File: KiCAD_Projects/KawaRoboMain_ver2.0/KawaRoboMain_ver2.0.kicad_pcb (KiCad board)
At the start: 2 copper layers, 65 x 75 mm, 128 parts, among them IC1 ATMEGA328P-A, P1 CONN_01X06, P10 CONN_01X02, P17 CONN_01X04, P19 CONN_01X01, P2 CONN_02X03, P21 CONN_01X01, P22 CONN_01X01, P3 CONN_01X06, P4 CONN_01X08, P5 CONN_01X06, P6 CONN_01X04, P7 CONN_01X01, P8 CONN_01X04, P9 CONN_01X03, Q1 MOSFET_N, Q10 MOSFET_N, Q11 MOSFET_N, Q12 MOSFET_N, Q13 MOSFET_N, Q14 MOSFET_N, Q17 MOSFET_N, Q2 MOSFET_N, Q3 MOSFET_N, Q4 MOSFET_N, Q5 MOSFET_N, Q6 MOSFET_N, Q7 MOSFET_N, Q8 MOSFET_N, Q9 MOSFET_N, SW1 SW_PUSH, SW2 SW_PUSH, SW3 SW_PUSH, SW6 SW_PUSH, SW7 SW_PUSH, U1 STM32F103_48, U10 NCP5359, U11 NCP5359, U15 NCP1117ST12T3G, U2 NCP1117ST33T3G, U3 NCP5359, U5 NCP5359, U8 NCP5359, U9 NCP5359, X1 CRYSTAL, X2 CRYSTAL

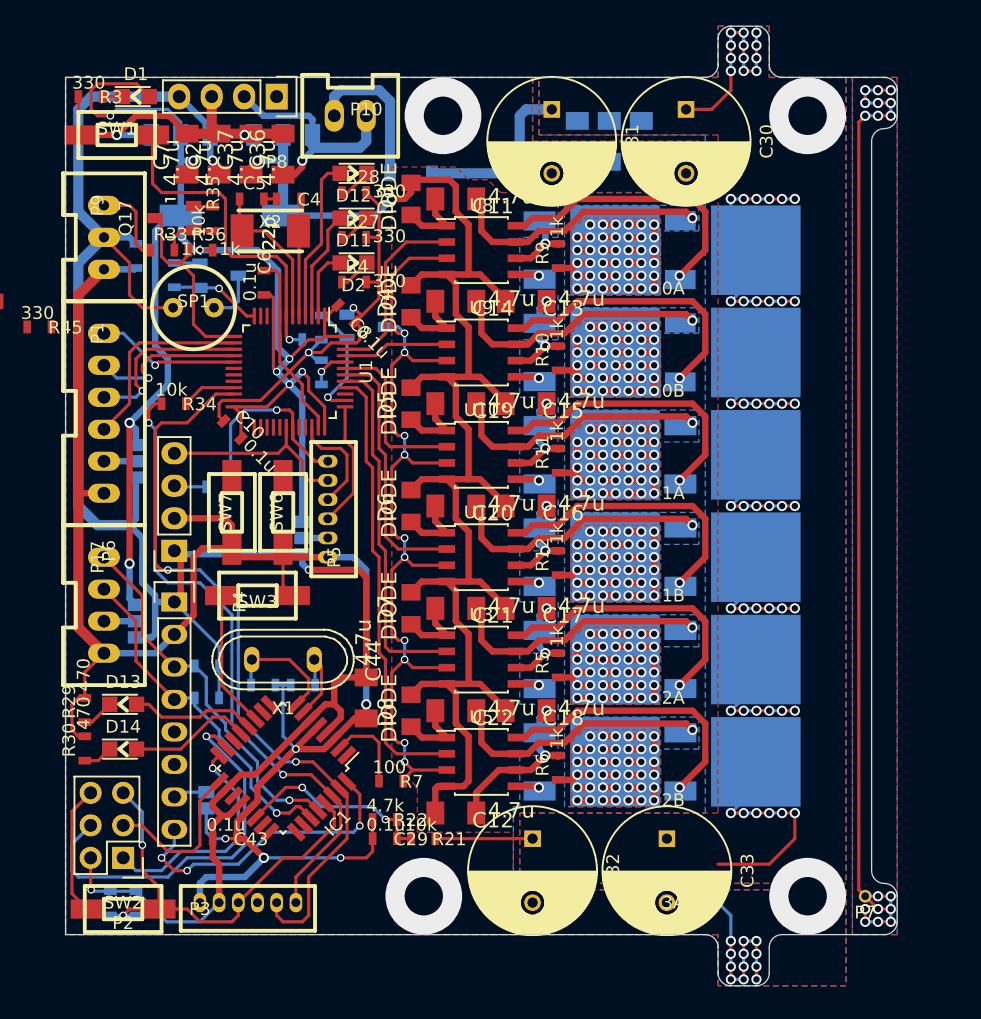
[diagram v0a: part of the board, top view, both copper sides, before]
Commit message: かわロボver2.0､中間電圧追加
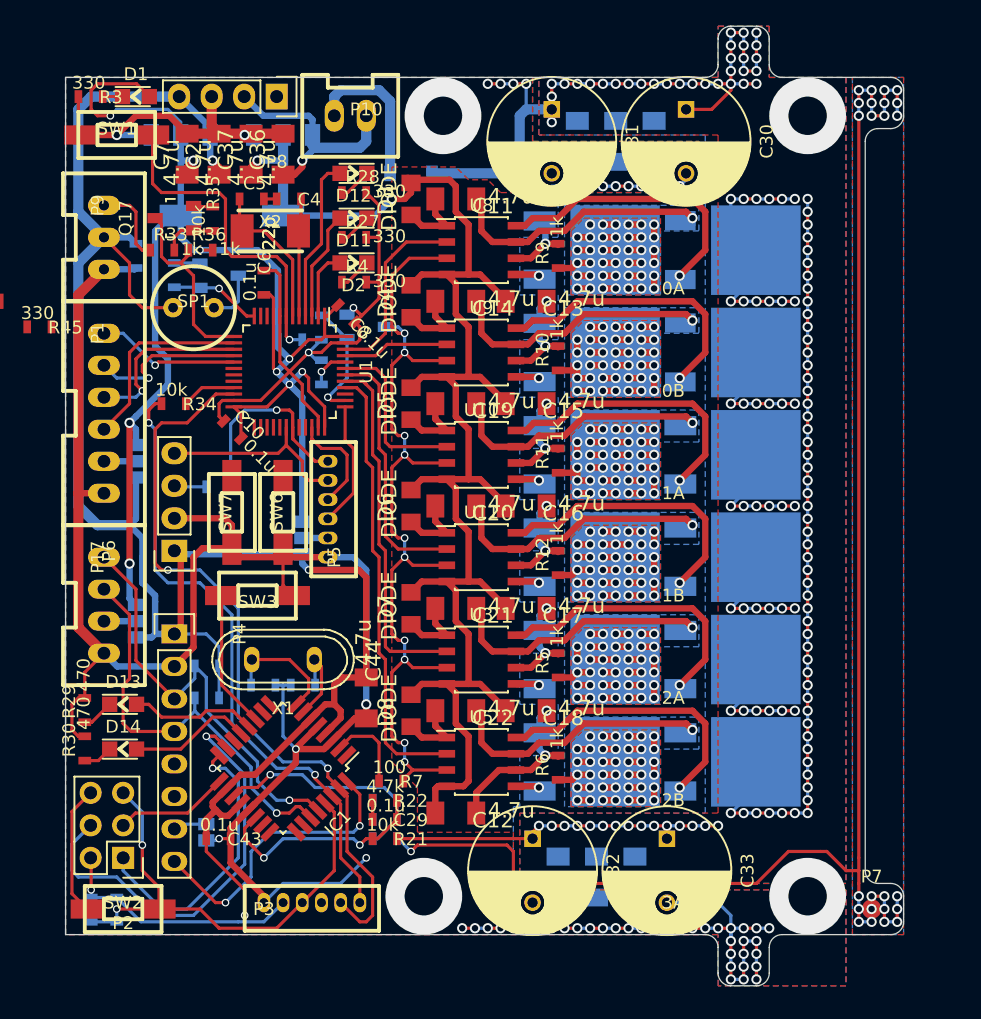
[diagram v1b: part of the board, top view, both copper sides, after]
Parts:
- added C1: 4.7u, RP_KiCAD_Libs:C3216_S, B.Cu at (60.5, 69.0)
- added C23: 0.1u, RP_KiCAD_Libs:C1608_WP_S, B.Cu at (41.0, 63.0)
- added C3: 4.7u, RP_KiCAD_Libs:C3216_S, B.Cu at (57.5, 69.0)
- added C9: 4.7u, RP_KiCAD_Libs:C3216_S, B.Cu at (54.5, 69.0)
- added R14: 4.7k, RP_KiCAD_Libs:C1608_WP_S, B.Cu at (41.0, 66.0)
- added R15: 4.7k, RP_KiCAD_Libs:C1608_WP_S, B.Cu at (41.0, 64.5)
- P7: footprint RP_KiCAD_Libs:testPin -> Measurement_Points:Measurement_Point_Round-SMD-Pad_Small
- moved P3 5.00 mm to (31.5, 71.0)
- moved R21 3.00 mm to (41.0, 66.0)
- moved JP1 2.50 mm to (27.0, 65.5)
- moved P4 2.50 mm to (24.5, 50.0)
- moved R19 1.58 mm to (18.0, 71.5)
- moved R32 1.58 mm to (20.0, 71.5)
- moved C29 1.50 mm to (41.0, 64.5)
- moved R22 1.50 mm to (41.0, 63.0)
- moved P7 1.12 mm to (79.0, 71.5)
- moved C40 1.00 mm to (62.0, 11.5)
- moved C43 0.50 mm to (28.0, 66.0)
- moved C45 0.50 mm to (59.0, 11.5)
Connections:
- IC1 pad 19: (no net) -> /cell_voltage
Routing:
- net +BATT: track 114.9 -> 197.3 mm, vias 54 -> 141
- net /BATT-SP: track 78.8 -> 123.8 mm, vias 18 -> 25
- net GND: track 305.4 -> 339.4 mm, vias 32 -> 66
- net /cell_voltage: track 0.00 -> 18.3 mm, vias 0 -> 1
- net +5V: track 166.4 -> 177.0 mm, vias 3 -> 4
- net /I2C_SDA: track 27.6 -> 32.9 mm
- net /SPI_MISO: track 18.7 -> 23.3 mm
- net /I2C_SCL: track 29.3 -> 33.6 mm
- net /SPI_SCK: track 12.7 -> 8.94 mm
- net /SPI_MOSI: track 31.3 -> 34.6 mm
- net /AT_RST: track 35.1 -> 38.3 mm
- net /batt_voltage: track 15.7 -> 17.7 mm
- net /INT0: track 24.9 -> 23.4 mm, vias 3 -> 2
- net /AT_RX: track 50.1 -> 49.5 mm
- net /AT_TX: track 59.8 -> 59.2 mm
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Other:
- board size 65 x 75 mm -> 65.5 x 75 mm

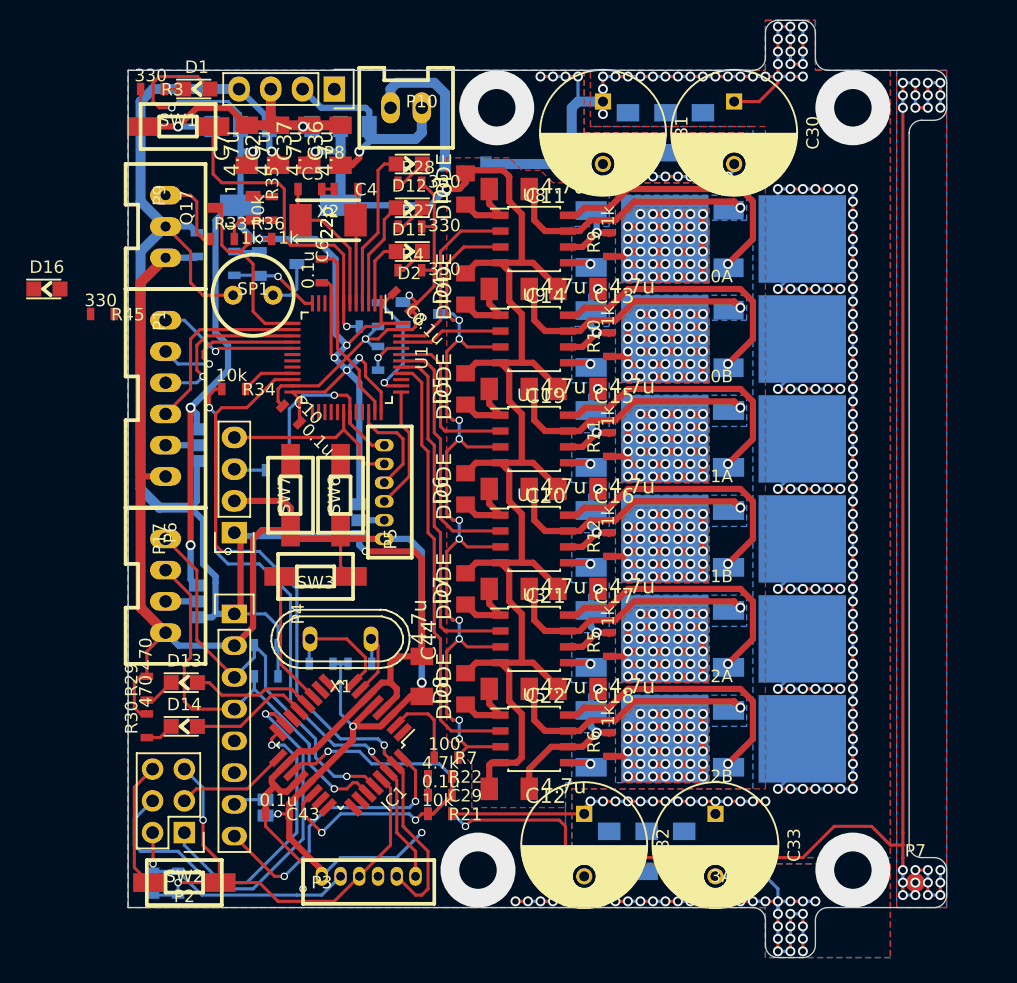
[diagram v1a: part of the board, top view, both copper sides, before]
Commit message: 中華DCDCやMPU6050､RSproブザーのライブラリ作った+2.0へ反映
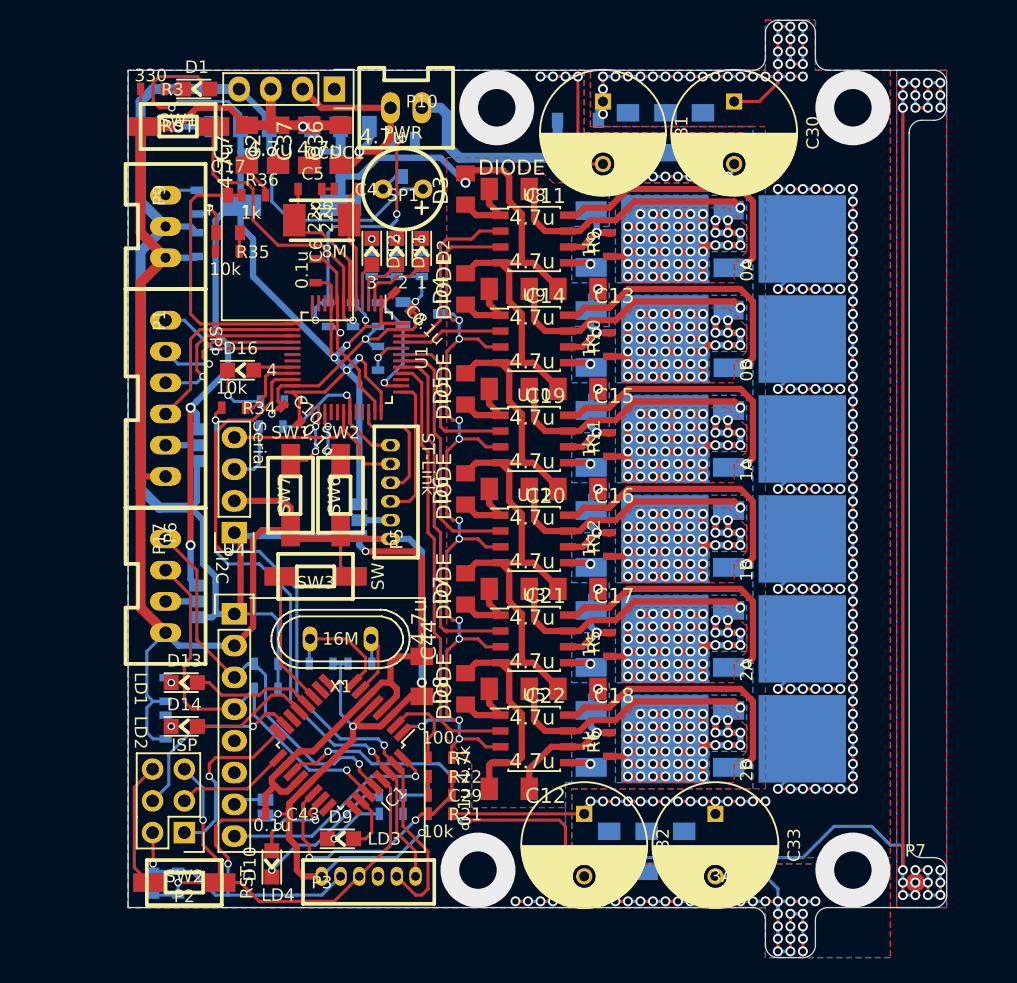
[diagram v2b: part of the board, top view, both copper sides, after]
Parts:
- removed P4: CONN_01X08, Socket_Strips:Socket_Strip_Straight_1x08_MPU6050
- removed P8: CONN_01X04, Socket_Strips:Socket_Strip_Straight_1x04
- added D10: LED, LEDs:LED_0805, F.Cu at (27.5, 70.0)
- added D9: LED, LEDs:LED_0805, F.Cu at (33.0, 68.0)
- added DCDC1: ChinaDC-DC, RP_KiCAD_Libs:ChinaDC-DC, F.Cu at (32.5, 8.00)
- added R16: 470, RP_KiCAD_Libs:C1608_WP_S, B.Cu at (37.0, 66.0)
- added R23: 470, RP_KiCAD_Libs:C1608_WP_S, B.Cu at (37.0, 64.5)
- added U4: MPU6050, RP_KiCAD_Libs:MPU-6050, F.Cu at (24.5, 50.0)
- R27, R28, R29, R30, R33, R4, R45: moved to B.Cu
- moved D16 16.8 mm to (25.0, 30.5)
- moved R45 15.2 mm to (27.5, 33.0), turned to 0 degrees
- moved SP1 14.7 mm to (38.0, 16.0), turned to 0 degrees
- moved Q14 13.1 mm to (38.0, 13.5), turned to 0 degrees
- moved D15 9.66 mm to (52.0, 10.5)
- moved R13 8.50 mm to (32.0, 26.0), turned to 270 degrees
- moved D12 7.62 mm to (35.5, 21.0), turned to 270 degrees
- moved R28 7.16 mm to (35.5, 22.0), turned to 270 degrees
- moved R35 4.95 mm to (24.0, 21.0), turned to 180 degrees
- moved D11 3.64 mm to (37.5, 21.0), turned to 270 degrees
- moved R33 3.61 mm to (21.5, 17.0), turned to 270 degrees
- moved R20 3.54 mm to (27.5, 35.0)
- moved R36 3.54 mm to (26.0, 16.5)
- moved R27 3.16 mm to (37.5, 22.0), turned to 270 degrees
- moved R18 1.50 mm to (27.0, 54.0)
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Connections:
- D16 pad 1: (no net) -> /STM_LED4
- IC1 pad 1: (no net) -> /Motor~SD
- IC1 pad 23: (no net) -> /AT_LED4
- IC1 pad 26: (no net) -> /AT_LED3
- P10 pad 1: Net-(D15-Pad1) -> /LOGIC_BATT
- P10 pad 2: /LOGIC_BATT -> Net-(D15-Pad1)
- SW6 pad 2: (no net) -> /STM_SW1
- SW7 pad 2: (no net) -> /STM_SW2
- U1 pad 20: (no net) -> /STM_LED4
- U1 pad 26: (no net) -> /STM_SW2
- U1 pad 27: (no net) -> /STM_SW1
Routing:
- net GND: track 339.4 -> 366.7 mm, vias 66 -> 72
- net /SPI_MOSI: track 34.6 -> 16.0 mm
- net /BEEP: track 7.18 -> 23.6 mm, vias 1 -> 3
- net +BATT: track 197.3 -> 182.4 mm, vias 141 -> 137
- net +5V: track 177.0 -> 189.4 mm
- net Net-(D10-Pad2): track 0.00 -> 11.6 mm, vias 0 -> 1
- net /STM_LED3: track 12.8 -> 3.41 mm
- net /SPI_MISO: track 23.3 -> 14.2 mm
- net /OUT_1_A: track 74.0 -> 82.2 mm, vias 42 -> 50
- net /OUT_2_A: track 77.4 -> 85.6 mm, vias 42 -> 50
- net /OUT_0_B: track 74.0 -> 82.2 mm, vias 42 -> 50
- net /OUT_0_A: track 74.6 -> 82.8 mm, vias 42 -> 50
- net /OUT_2_B: track 67.6 -> 75.6 mm, vias 42 -> 50
- net /OUT_1_B: track 71.1 -> 79.1 mm, vias 42 -> 50
- net /AT_LED4: track 0.00 -> 7.53 mm, vias 0 -> 2
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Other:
- board text added: "1"
- board text added: "16M"
- board text added: "2"
- board text added: "3"
- board text added: "3.3V"
- board text added: "4"
- board text added: "5V"
- board text added: "8M"
- board text added: "I2C"
- board text added: "ISP"
- board text added: "LD1"
- board text added: "LD2"
- board text added: "LD3"
- board text added: "LD4"
- board text added: "PWR"
- board text added: "RST"
- board text added: "SPI"
- board text added: "ST-Link"
- board text added: "SW"
- board text added: "SW1"
- board text added: "SW2"
- board text added: "Serial"

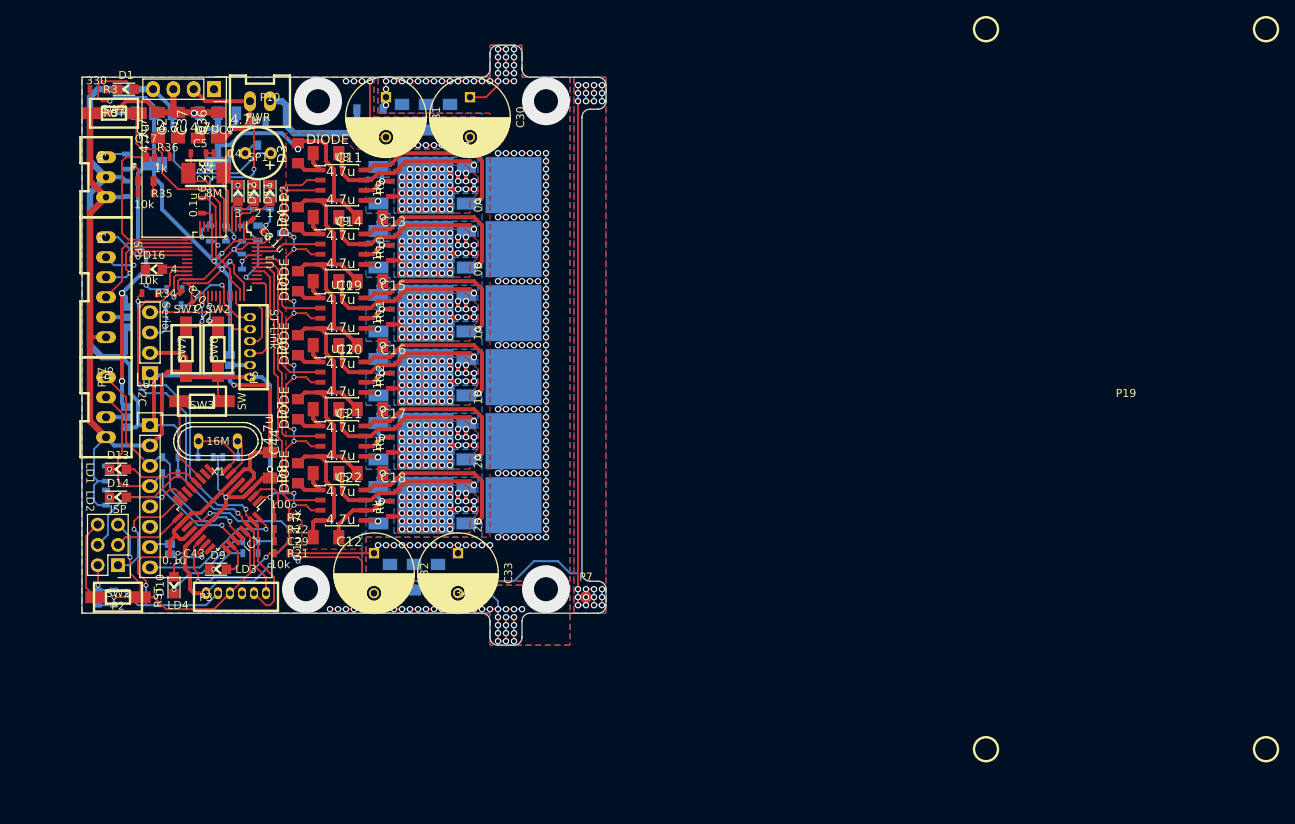
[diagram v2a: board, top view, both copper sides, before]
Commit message: 面実装ブザー付けた
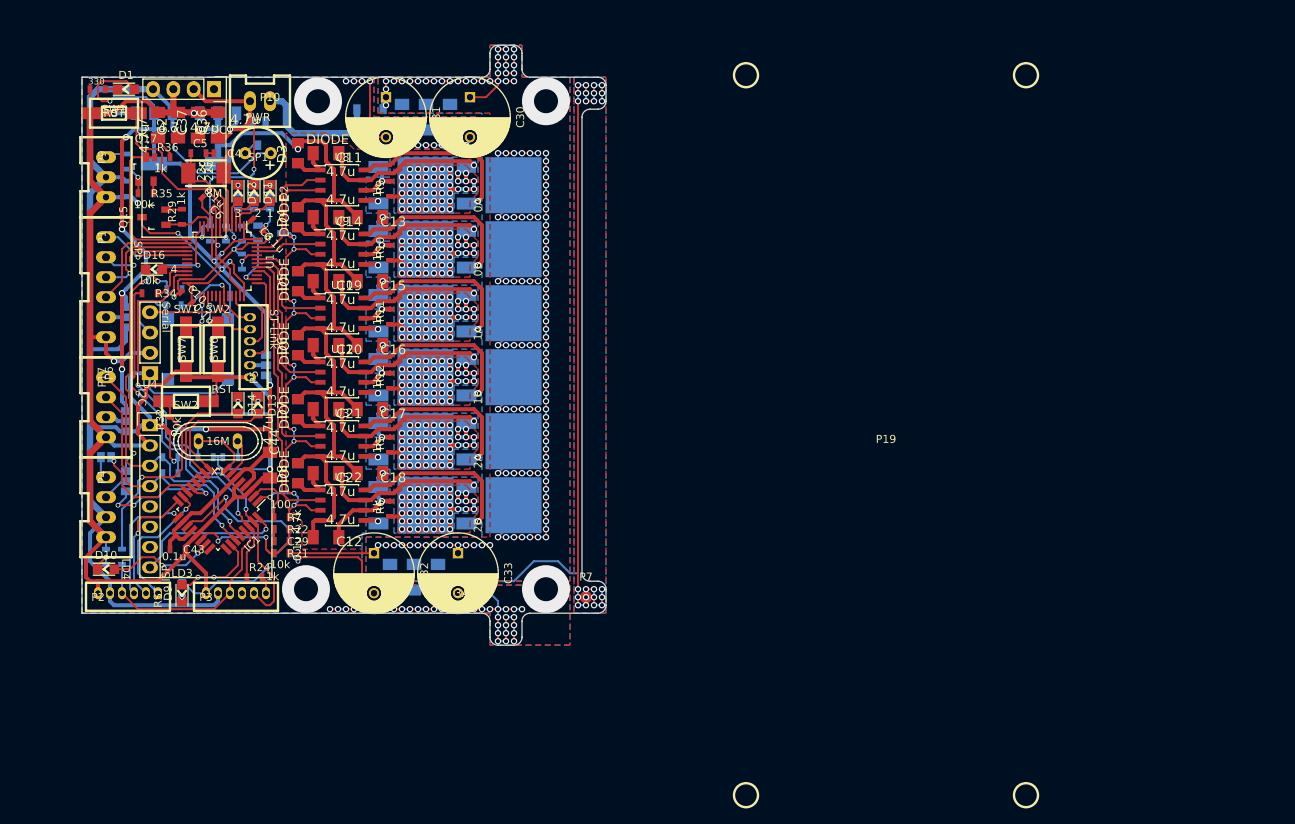
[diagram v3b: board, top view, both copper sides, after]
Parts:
- removed R30: 470, RP_KiCAD_Libs:C1608_WP_S
- removed SW3: SW_PUSH, Buttons_Switches_SMD:RP_SMD_Button
- added JP4: JUMPER, Connect:GS2, B.Cu at (19.0, 54.0)
- added P4: CONN_01X04, RP_KiCAD_Connector:XA_4T, F.Cu at (19.0, 56.5)
- added Q15: MOSFET_N, TO_SOT_Packages_SMD:SOT-23_Handsoldering, F.Cu at (25.0, 24.0)
- added R24: 1k, RP_KiCAD_Libs:C1608_WP_S, F.Cu at (37.5, 69.0)
- added R25: 470, RP_KiCAD_Libs:C1608_WP_S, B.Cu at (38.0, 47.5)
- added R26: 470, RP_KiCAD_Libs:C1608_WP_S, B.Cu at (35.5, 47.5)
- added SP2: SPEAKER, RP_KiCAD_Libs:UGCT7525AN4, B.Cu at (30.5, 40.5)
- JP1: value JUMPER -> JUMPER3; footprint Connect:GS2 -> Connect:GS3
- P2: value CONN_02X03 -> CONN_01X06; footprint Pin_Headers:Pin_Header_Straight_2x03 -> RP_KiCAD_Connector:ZH_6T
- R29: value 470 -> 1k; moved to F.Cu
- R32: moved to F.Cu
- moved R29 33.4 mm to (28.5, 24.0), turned to 90 degrees
- moved P19 30.5 mm to (116.5, 51.2)
- moved SW2 25.9 mm to (29.0, 47.0), turned to 0 degrees
- moved R32 22.6 mm to (27.0, 50.0), turned to 90 degrees
- moved D13 19.2 mm to (38.0, 47.5), turned to 270 degrees
- moved D14 18.9 mm to (35.5, 47.5), turned to 270 degrees
- moved R23 18.1 mm to (19.0, 66.5), turned to 90 degrees
- moved JP1 10.1 mm to (21.5, 57.0), turned to 0 degrees
- moved R16 9.62 mm to (28.5, 70.5), turned to 90 degrees
- moved D10 8.73 mm to (19.0, 68.0), turned to 0 degrees
- moved R19 5.83 mm to (21.0, 66.5), turned to 90 degrees
- moved D9 5.41 mm to (28.5, 71.0), turned to 90 degrees
- moved JP2 4.50 mm to (39.0, 42.5)
- moved P2 4.30 mm to (18.0, 71.0), turned to 0 degrees
- moved C6 0.79 mm to (31.8, 22.2), turned to 135 degrees
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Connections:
- IC1 pad 10: (no net) -> /AT_LED2
- IC1 pad 11: /AT_SW1 -> (no net)
- IC1 pad 12: /AT_LED1 -> (no net)
- IC1 pad 13: /AT_LED2 -> /SS_TX
- IC1 pad 14: (no net) -> /SS_RX
- IC1 pad 9: (no net) -> /AT_LED1
- JP1 pad 1: Net-(JP1-Pad1) -> /SS_TX
- JP1 pad 2: GND -> Net-(JP1-Pad2)
- P2 pad 1: /SPI_MISO -> GND
- P2 pad 3: /SPI_SCK -> /AT_RST
- P2 pad 4: /SPI_MOSI -> /SPI_SCK
- P2 pad 5: /AT_RST -> /SPI_MISO
- P2 pad 6: GND -> /SPI_MOSI
- P3 pad 6: /AT_RX -> Net-(P3-Pad6)
- Q14 pad G: /BEEP -> /BEEP1
- R13 pad 1: /BEEP -> /BEEP1
- R19 pad 1: +5V -> /AT_RST
- R19 pad 2: /AT_RST -> Net-(R19-Pad2)
- R29 pad 1: Net-(D13-Pad2) -> /BEEP0
- R32 pad 2: /AT_RST -> Net-(R19-Pad2)
- SW2 pad 2: /AT_RST -> Net-(R19-Pad2)
- U1 pad 10: (no net) -> /BEEP0
- U1 pad 11: (no net) -> /BEEP1
- U1 pad 12: /BEEP -> /EX_TX
- U4 pad 7: Net-(JP1-Pad1) -> (no net)
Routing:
- net /EX_TX: track 0.00 -> 39.2 mm, vias 0 -> 3
- net Net-(R19-Pad2): track 0.00 -> 25.2 mm, vias 0 -> 1
- net /BEEP1: track 0.00 -> 23.7 mm, vias 0 -> 3
- net /BEEP: track 23.6 -> 0.00 mm, vias 3 -> 0
- net +5V: track 189.4 -> 212.7 mm, vias 4 -> 5
- net GND: track 366.7 -> 388.3 mm
- net Net-(Q15-PadD): track 0.00 -> 19.5 mm, vias 0 -> 1
- net /SS_TX: track 0.00 -> 16.3 mm, vias 0 -> 3
- net /SS_RX: track 0.00 -> 13.8 mm, vias 0 -> 1
- net +3.3V: track 123.8 -> 137.2 mm, vias 9 -> 11
- net /AT_SW1: track 10.7 -> 0.00 mm
- net /AT_RST: track 38.3 -> 27.9 mm, vias 2 -> 0
- net Net-(D10-Pad2): track 11.6 -> 2.83 mm
- net /BEEP0: track 0.00 -> 6.65 mm
- net /SPI_SCK: track 8.94 -> 15.6 mm, vias 0 -> 1
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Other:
- board text removed: "LD1"
- board text removed: "LD2"
- board text removed: "SW"

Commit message: ver1.2設計してる
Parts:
- added D17: DIODE, RP_KiCAD_Libs:C2012, B.Cu at (16.8, 59.0)
- D15: footprint Diodes_SMD:SOD-123 -> RP_KiCAD_Libs:C3216_S
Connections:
- P4 pad 2: +5V -> Net-(D17-Pad1)
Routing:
- net Net-(D17-Pad1): track 0.00 -> 3.35 mm
- net +5V: track 212.7 -> 212.4 mm, vias 5 -> 6
